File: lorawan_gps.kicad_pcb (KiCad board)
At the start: 2 copper layers, 95 x 20 mm, 105 parts, among them IC1 TPS61201, J1 MICRO-USB, P1 BL_PAD, P11 CONN_01X04, P2 SWD_DAT, P3 SWD_CLK, P4 SWD_3V3, P5 SWD_GND, P6 SWD_RST, Q1 Q_PMOS_GSD, SW1 SW_PUSH, SW2 SW_PUSH, U1 SHT21, U2 MPU-9250, U3 RFM9xW, U4 SAMD21E17A, U5 MAX-M8, Y1 32.768kHz

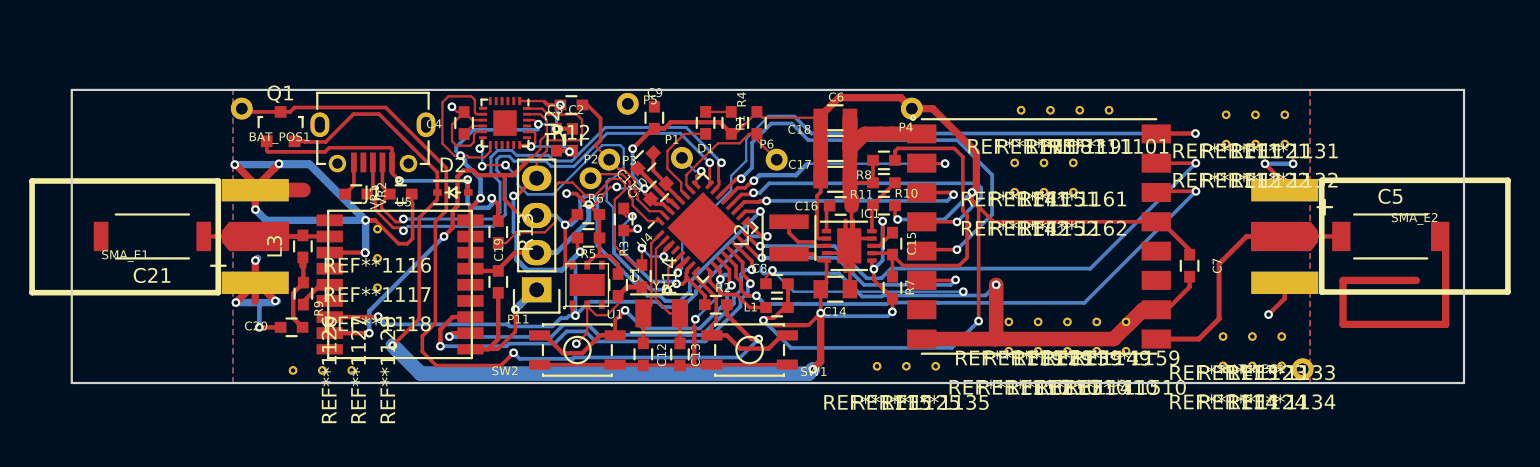
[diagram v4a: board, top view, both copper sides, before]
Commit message: Fixed layout, updated RF track width, switch footprint fixed, layout around accelerometer fixed
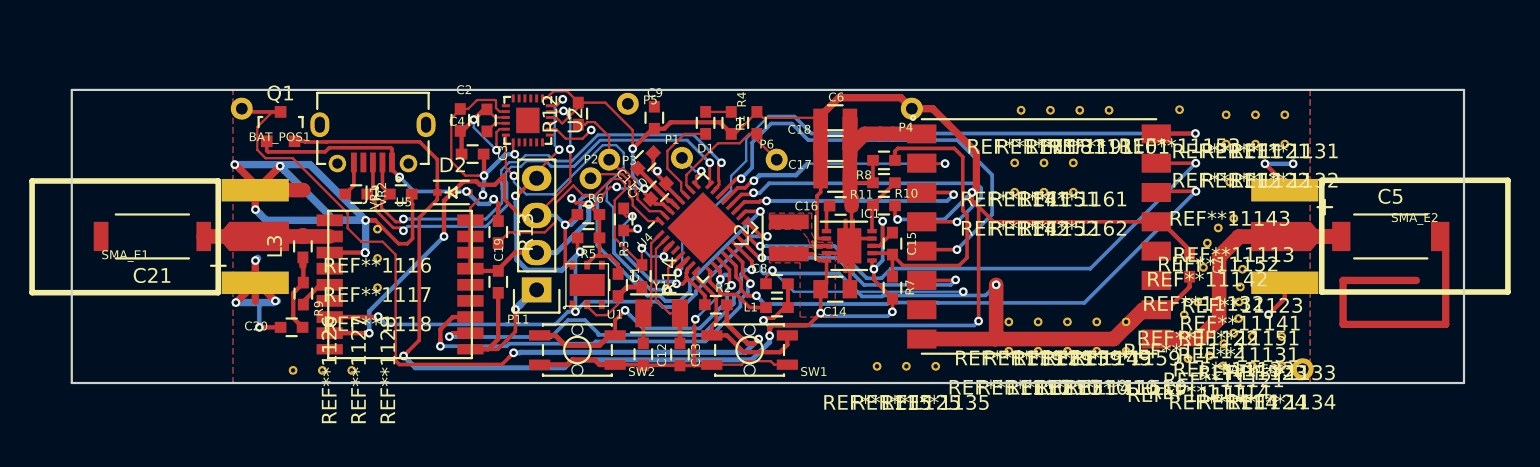
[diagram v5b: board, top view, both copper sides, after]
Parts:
- added REF**11112: Stitch_Via, Oddities:Stitch_Via, F.Cu at (170.9, 85.3)
- added REF**11113: Stitch_Via, Oddities:Stitch_Via, F.Cu at (174.3, 78.8)
- added REF**11114: Stitch_Via, Oddities:Stitch_Via, F.Cu at (172.6, 88.1)
- added REF**11121: Stitch_Via, Oddities:Stitch_Via, F.Cu at (173.6, 87.3)
- added REF**11122: Stitch_Via, Oddities:Stitch_Via, F.Cu at (171.8, 84.5)
- added REF**11123: Stitch_Via, Oddities:Stitch_Via, F.Cu at (174.9, 82.2)
- added REF**11131: Stitch_Via, Oddities:Stitch_Via, F.Cu at (174.6, 85.6)
- added REF**11132: Stitch_Via, Oddities:Stitch_Via, F.Cu at (172.2, 82.1)
- added REF**11133: Stitch_Via, Oddities:Stitch_Via, F.Cu at (174.3, 86.6)
- added REF**11141: Stitch_Via, Oddities:Stitch_Via, F.Cu at (174.7, 83.5)
- added REF**11142: Stitch_Via, Oddities:Stitch_Via, F.Cu at (172.5, 80.5)
- added REF**11143: Stitch_Via, Oddities:Stitch_Via, F.Cu at (174.0, 76.3)
- added REF**11151: Stitch_Via, Oddities:Stitch_Via, F.Cu at (174.7, 84.5)
- added REF**11152: Stitch_Via, Oddities:Stitch_Via, F.Cu at (173.2, 79.4)
- added REF**11153: Stitch_Via, Oddities:Stitch_Via, F.Cu at (170.6, 71.3)
- SW1, SW2: footprint Buttons_Switches_SMD:SW_SPST_EVQP2 -> TL1014BF180QG:TL1014BF180QG
- moved C2 7.77 mm to (121.5, 72.0)
- moved C3 5.80 mm to (122.3, 74.4), turned to 180 degrees
- moved REF**11111 2.83 mm to (171.2, 88.3)
- moved C4 1.57 mm to (123.3, 72.1)
- moved U2 1.57 mm to (126.1, 72.1)
- moved R12 0.75 mm to (129.6, 71.6), turned to 90 degrees
- renumbered REF**1113 to REF**11111
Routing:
- net Net-(C5-Pad1): track 20.0 -> 28.6 mm
- net Net-(C14-Pad1): track 85.0 -> 78.0 mm
- net /MCU/MPU_SDA: track 64.2 -> 60.0 mm, vias 5 -> 7
- net +3V3: track 160.7 -> 157.1 mm, vias 14 -> 12
- net Net-(IC1-Pad3): track 3.89 -> 1.28 mm
- net Net-(D2-Pad2): track 23.0 -> 20.6 mm
- net /Battery and USB Connector/D+: track 35.7 -> 33.5 mm
- net /Battery and USB Connector/D-: track 36.6 -> 34.5 mm
- net /9axis/INT_9AXIS: track 29.8 -> 27.8 mm, vias 4 -> 2
- net /MCU/MPU_SCL: track 61.2 -> 63.1 mm, vias 4 -> 6
- net GND: track 224.8 -> 223.0 mm
- net /Battery and USB Connector/V_USB_Sense: track 24.0 -> 22.8 mm
- net /GPS/GPS_FEEDER: track 11.6 -> 12.4 mm
- net Net-(P3-Pad1): track 11.4 -> 10.6 mm
- net Net-(SW1-Pad1): track 11.0 -> 11.6 mm
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- added copper zone on F.Cu, net Net-(C14-Pad1)
- added copper zone on F.Cu, net Net-(IC1-Pad3)
